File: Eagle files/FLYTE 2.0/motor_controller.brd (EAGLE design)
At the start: 160 x 100 mm, 21 parts, among them J1 XT60PW-F

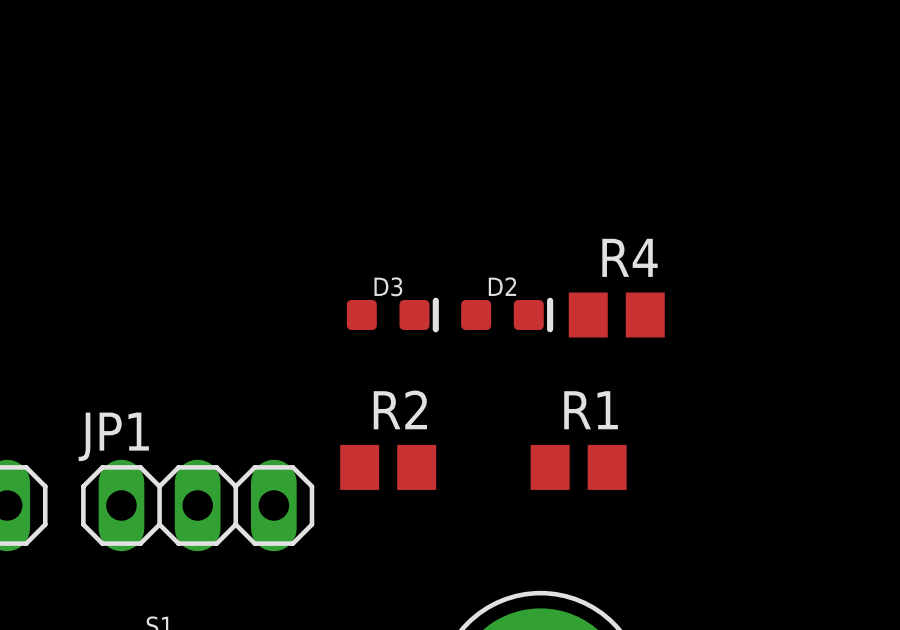
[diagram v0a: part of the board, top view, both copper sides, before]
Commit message: Finish schematic for motor controller
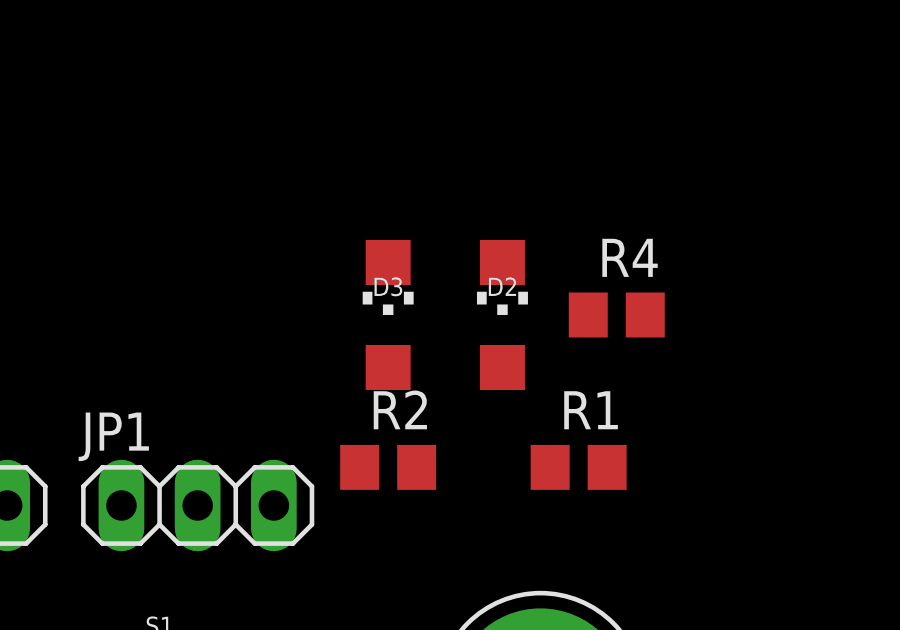
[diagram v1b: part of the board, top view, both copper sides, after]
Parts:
- D2, D3: device SparkFun-LED:LED-0603 -> led:CHIPLED_1206
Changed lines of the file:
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@@
 <attribute name="VALUE" x="-65.532" y="68.326" size="1.27" layer="27" ratio="10"/>
 </element>
-<element name="D2" library="SparkFun-LED" package="LED-0603" value="" x="-19.05" y="85.09" smashed="yes">
+<element name="D2" library="led" library_urn="urn:adsk.eagle:library:259" package="CHIPLED_1206" package3d_urn="urn:adsk.eagle:package:15823/2" value="" x="-19.05" y="85.09" smashed="yes">
 <attribute name="NAME" x="-19.05" y="85.725" size="0.6096" layer="25" font="vector" ratio="20" align="bottom-center"/>
+<attribute name="POPULARITY" value="28" x="-19.05" y="85.09" size="1.778" layer="27" display="off"/>
 <attribute name="VALUE" x="-19.05" y="84.455" size="0.6096" layer="27" font="vector" ratio="20" align="top-center"/>
 </element>
-<element name="D3" library="SparkFun-LED" package="LED-0603" value="" x="-22.86" y="85.09" smashed="yes">
+<element name="D3" library="led" library_urn="urn:adsk.eagle:library:259" package="CHIPLED_1206" package3d_urn="urn:adsk.eagle:package:15823/2" value="" x="-22.86" y="85.09" smashed="yes">
 <attribute name="NAME" x="-22.86" y="85.725" size="0.6096" layer="25" font="vector" ratio="20" align="bottom-center"/>
+<attribute name="POPULARITY" value="28" x="-22.86" y="85.09" size="1.778" layer="27" display="off"/>
 <attribute name="VALUE" x="-22.86" y="84.455" size="0.6096" layer="27" font="vector" ratio="20" align="top-center"/>
 </element>
@@
 <contactref element="D2" pad="C"/>
 <contactref element="U1" pad="P$22"/>
-<wire x1="-15.4" y1="7.62" x2="-18.173" y2="85.09" width="0" layer="19" extent="1-1"/>
+<wire x1="-15.4" y1="7.62" x2="-19.05" y2="86.84" width="0" layer="19" extent="1-1"/>
 </signal>
 <signal name="N$6">
 <contactref element="U1" pad="P$21"/>
 <contactref element="D3" pad="C"/>
-<wire x1="-15.4" y1="5.08" x2="-21.983" y2="85.09" width="0" layer="19" extent="1-1"/>
+<wire x1="-15.4" y1="5.08" x2="-22.86" y2="86.84" width="0" layer="19" extent="1-1"/>
 </signal>
 <signal name="N$7">
 <contactref element="R3" pad="1"/>
 <contactref element="D2" pad="A"/>
-<wire x1="-64.45" y1="77.47" x2="-19.927" y2="85.09" width="0" layer="19" extent="1-1"/>
+<wire x1="-64.45" y1="77.47" x2="-19.05" y2="83.34" width="0" layer="19" extent="1-1"/>
 </signal>
 <signal name="N$8">
 <contactref element="R4" pad="1"/>
 <contactref element="D3" pad="A"/>
-<wire x1="-23.737" y1="85.09" x2="-16.19" y2="85.09" width="0" layer="19" extent="1-1"/>
+<wire x1="-22.86" y1="83.34" x2="-16.19" y2="85.09" width="0" layer="19" extent="1-1"/>
 </signal>
 </signals>
